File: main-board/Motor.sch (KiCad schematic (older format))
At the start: 0 parts

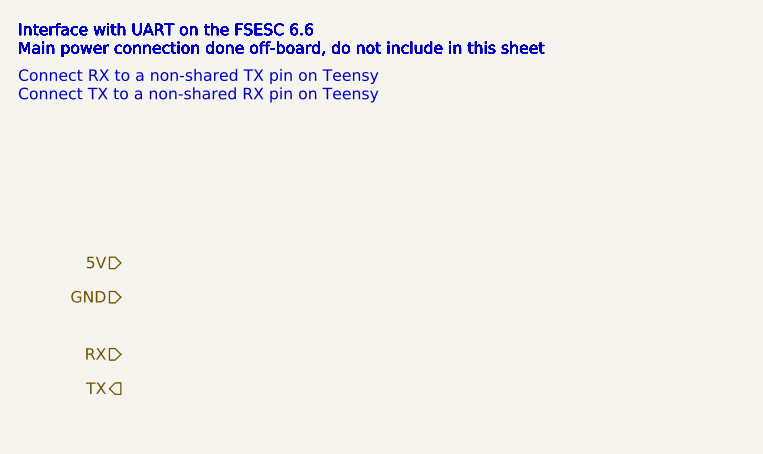
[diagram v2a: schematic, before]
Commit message: Subsheets
Added motor drivers, cooling fans, and openlog
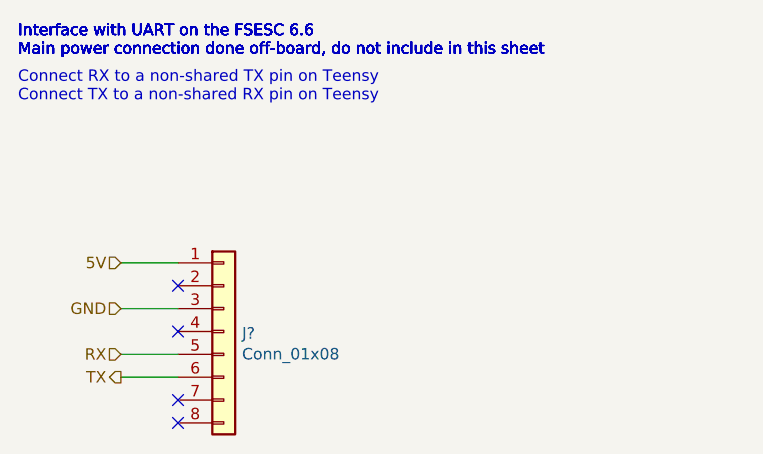
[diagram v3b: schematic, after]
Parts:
- added J?: Conn_01x08, symbol Connector_Generic:Conn_01x08
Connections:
- net 5V: now also J?.1 (Pin_1)
- net GND: now also J?.3 (Pin_3)
- net RX: now also J?.5 (Pin_5)
- net TX: now also J?.6 (Pin_6)
- no-connect marks 0 -> 4
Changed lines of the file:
@@
 EESchema Schematic File Version 4
+LIBS:main-board-cache
 EELAYER 30 0
 EELAYER END
 $Descr A4 11693 8268
 encoding utf-8
-Sheet 4 23
+Sheet 9 23
 Title ""
 Date ""
@@
 Text HLabel 5450 2900 0    50   Input ~ 0
 RX
-Text HLabel 5450 3050 0    50   Output ~ 0
+Text HLabel 5450 3000 0    50   Output ~ 0
 TX
 Text Notes 5000 1600 0    50   ~ 0
 Interface with UART on the FSESC 6.6\nMain power connection done off-board, do not include in this sheet
-Text HLabel 5450 2650 0    50   Input ~ 0
+Text HLabel 5450 2700 0    50   Input ~ 0
 GND
 Text Notes 5000 1600 0    50   ~ 0
@@
 Text Notes 5000 1800 0    50   ~ 0
 Connect RX to a non-shared TX pin on Teensy\nConnect TX to a non-shared RX pin on Teensy
+NoConn ~ 5700 3200
+NoConn ~ 5700 3100
+NoConn ~ 5700 2800
+NoConn ~ 5700 2600
+Wire Wire Line
+	5700 2700 5450 2700
+Wire Wire Line
+	5450 3000 5700 3000
+Wire Wire Line
+	5700 2900 5450 2900
+Wire Wire Line
+	5700 2500 5450 2500
+$Comp
+L Connector_Generic:Conn_01x08 J?
+U 1 1 60AFA1EC
+P 5900 2800
+AR Path="/6074EB9F/60AFA1EC" Ref="J?"  Part="1"
+AR Path="/6074E0BF/60AFA1EC" Ref="J?"  Part="1"
+AR Path="/6074EE19/60AFA1EC" Ref="J?"  Part="1"
+AR Path="/6074ED4A/60AFA1EC" Ref="J?"  Part="1"
+AR Path="/6074EA58/60AFA1EC" Ref="J?"  Part="1"
+AR Path="/6074E8BC/60AFA1EC" Ref="J?"  Part="1"
+F 0 "J?" H 5980 2792 50  0000 L CNN
+F 1 "Conn_01x08" H 5980 2701 50  0000 L CNN
+F 2 "" H 5900 2800 50  0001 C CNN
+F 3 "~" H 5900 2800 50  0001 C CNN
+	1    5900 2800
+	1    0    0    -1
+$EndComp
 $EndSCHEMATC
